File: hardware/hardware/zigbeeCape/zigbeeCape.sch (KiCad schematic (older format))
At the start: 46 parts

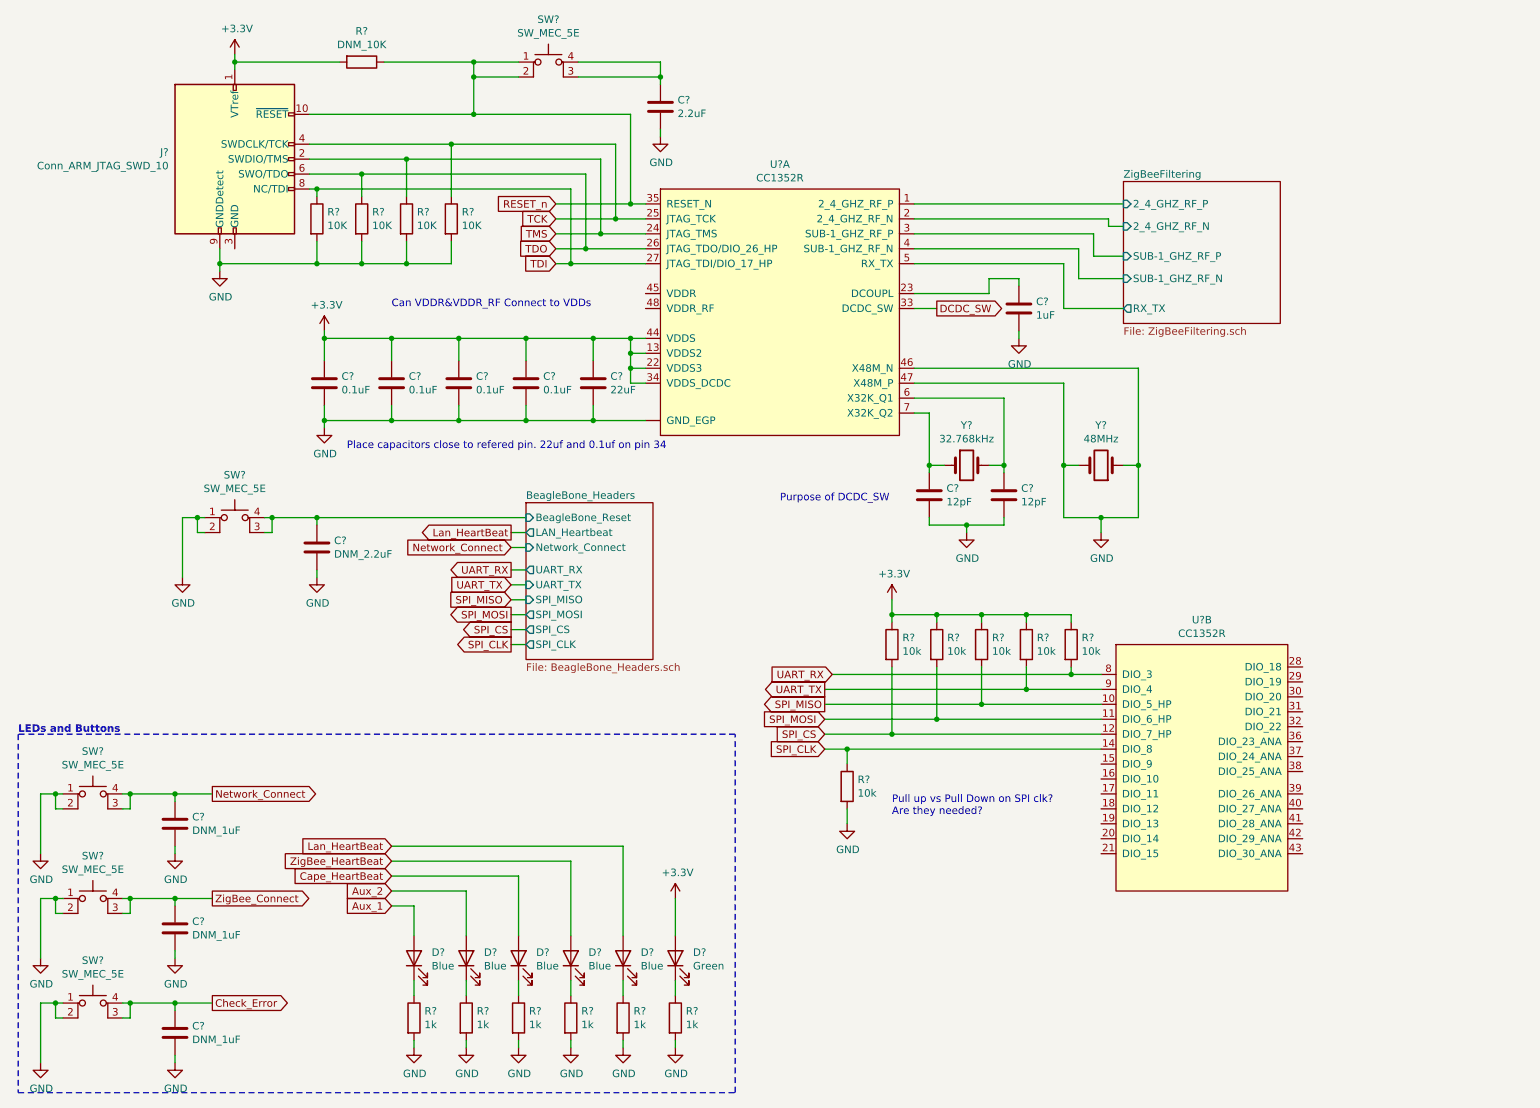
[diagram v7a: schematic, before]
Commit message: Added I2C pins, added signal wires to zigbee micro, fixed reset pin error
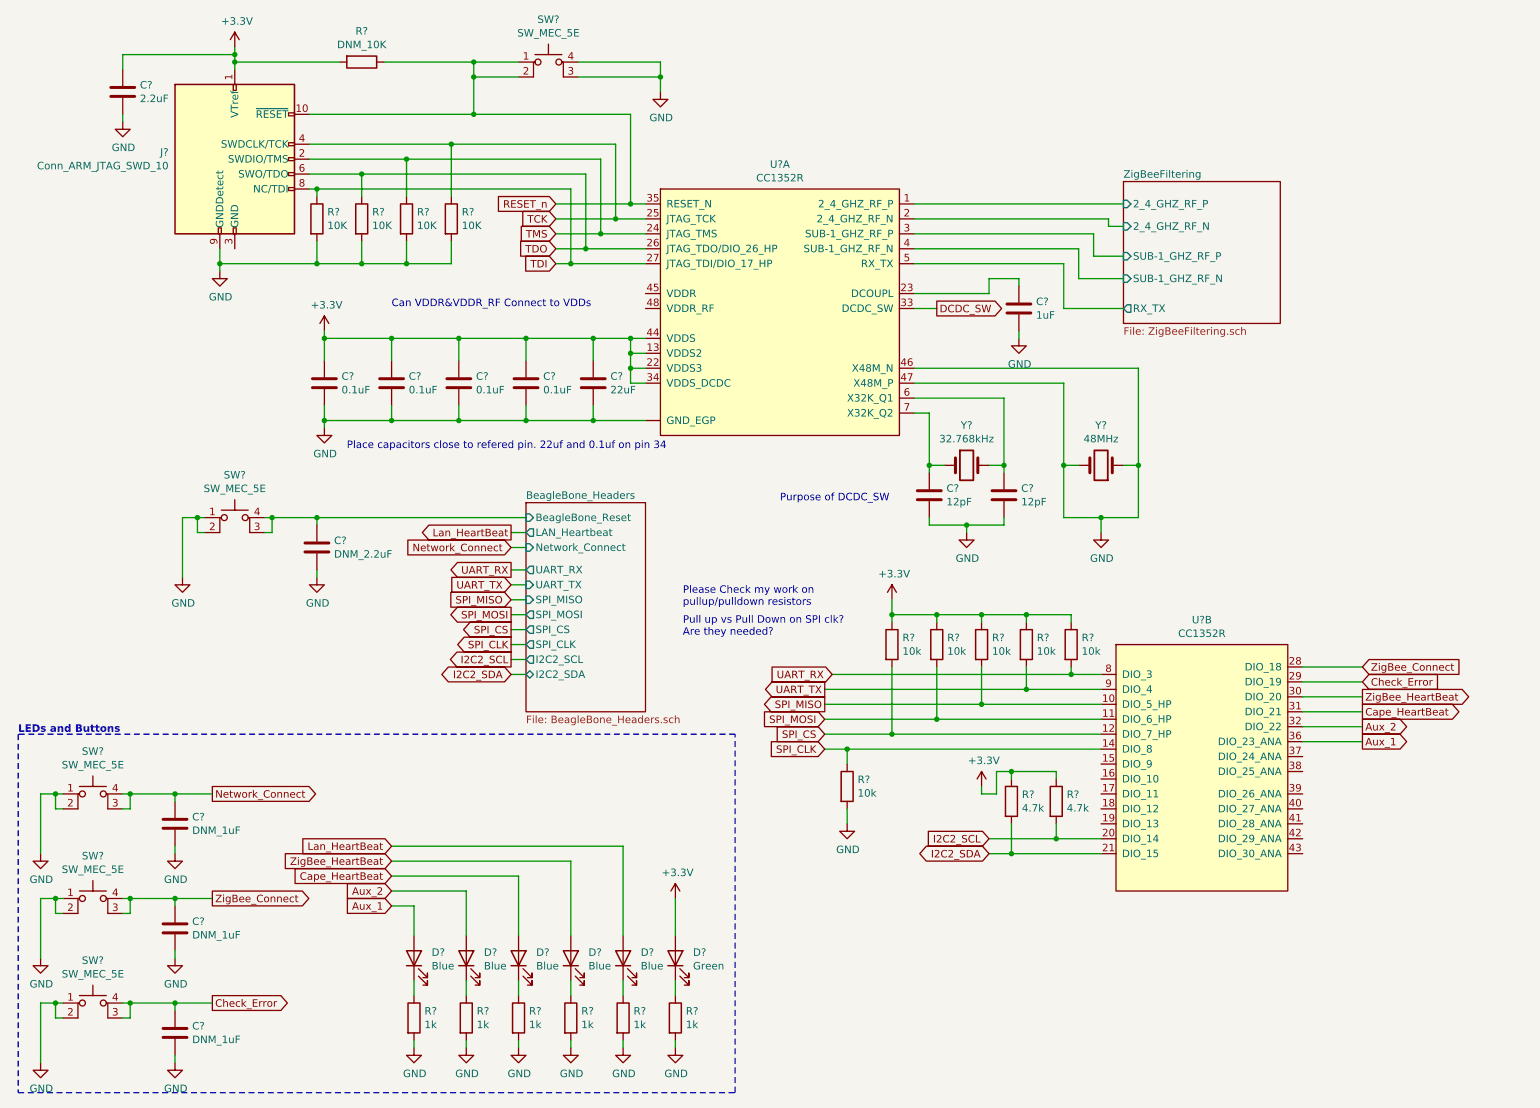
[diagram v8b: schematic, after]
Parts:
- added R? (x2): 4.7k, symbol Device:R
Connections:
- net +3V3: now also C?.1, R?.1, R?.1
- net Aux_1: now also U?.36 (DIO_23_ANA)
- net Aux_2: now also U?.32 (DIO_22)
- net Cape_HeartBeat: now also U?.31 (DIO_21)
- net Check_Error: now also U?.29 (DIO_19)
- net GND: now also SW?.3 (K), SW?.4 (A)
- net ZigBee_Connect: now also U?.28 (DIO_18)
- net ZigBee_HeartBeat: now also U?.30 (DIO_20)
- net I2C2_SCL: now reaches U?.20 (DIO_14)
- net I2C2_SCL: now also R?.2
- net I2C2_SDA: now reaches U?.21 (DIO_15)
- net I2C2_SDA: now also R?.2
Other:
- note added: "Please Check my work on \npullup/pulldown resistors"
- moved on the sheet: C?
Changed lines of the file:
@@
 Purpose of DCDC_SW
 $Sheet
-S 4000 3750 850  1050
+S 4000 3750 800  1400
 U 6087B849
 F0 "BeagleBone_Headers" 50
@@
 F9 "UART_TX" I L 4000 4300 50
 F10 "SPI_CLK" O L 4000 4700 50
+F11 "I2C2_SCL" O L 4000 4800 50
+F12 "I2C2_SDA" B L 4000 4900 50
 $EndSheet
 Wire Wire Line
@@
 	1    2900 800
 	0    1    1    0
-$EndComp
-$Comp
-L power:+3.3V #PWR?
-U 1 1 608A2617
-P 2050 750
-F 0 "#PWR?" H 2050 600 50  0001 C CNN
-F 1 "+3.3V" H 2065 923 50  0000 C CNN
-F 2 "" H 2050 750 50  0001 C CNN
-F 3 "" H 2050 750 50  0001 C CNN
-	1    2050 750
-	1    0    0    -1
 $EndComp
 $Comp
@@
 	4200 1850 4600 1850
 Connection ~ 4600 1850
-Wire Wire Line
-	2050 850  2050 800
 Connection ~ 3100 2650
 Connection ~ 3100 3200
@@
 Wire Wire Line
 	2550 1150 3650 1150
-Wire Wire Line
-	2050 800  2750 800
-Connection ~ 2050 800
-Wire Wire Line
-	2050 800  2050 750
 Wire Wire Line
 	3050 800  3650 800
@@
 L Device:C C?
 U 1 1 60A4B344
-P 4900 1100
-F 0 "C?" H 5015 1146 50  0000 L CNN
-F 1 "2.2uF" H 5015 1055 50  0000 L CNN
-F 2 "" H 4938 950 50  0001 C CNN
-F 3 "~" H 4900 1100 50  0001 C CNN
-	1    4900 1100
+P 1300 1000
+F 0 "C?" H 1415 1046 50  0000 L CNN
+F 1 "2.2uF" H 1415 955 50  0000 L CNN
+F 2 "" H 1338 850 50  0001 C CNN
+F 3 "~" H 1300 1000 50  0001 C CNN
+	1    1300 1000
 	1    0    0    -1
 $EndComp
 Wire Wire Line
 	4350 900  4900 900
-Wire Wire Line
-	4900 900  4900 950
 $Comp
 L power:GND #PWR?
 U 1 1 60A55AE5
-P 4900 1300
-F 0 "#PWR?" H 4900 1050 50  0001 C CNN
-F 1 "GND" H 4905 1127 50  0000 C CNN
-F 2 "" H 4900 1300 50  0001 C CNN
-F 3 "" H 4900 1300 50  0001 C CNN
-	1    4900 1300
-	1    0    0    -1
-$EndComp
-Wire Wire Line
-	4900 1300 4900 1250
+P 4900 1000
+F 0 "#PWR?" H 4900 750 50  0001 C CNN
+F 1 "GND" H 4905 827 50  0000 C CNN
+F 2 "" H 4900 1000 50  0001 C CNN
+F 3 "" H 4900 1000 50  0001 C CNN
+	1    4900 1000
+	1    0    0    -1
+$EndComp
 Wire Wire Line
 	4350 800  4900 800
 Wire Wire Line
 	4900 800  4900 900
-Connection ~ 4900 900
 $Comp
 L Switch:SW_MEC_5E SW?
@@
 Text GLabel 6000 5400 0    50   Input ~ 0
 SPI_CLK
-Text Notes 6450 5850 0    50   ~ 0
+Text Notes 5050 4650 0    50   ~ 0
 Pull up vs Pull Down on SPI clk?\nAre they needed?
-$Comp
-L Device:R R?
-U 1 1 60B56235
-P 7650 4700
-F 0 "R?" H 7720 4746 50  0000 L CNN
-F 1 "10k" H 7720 4655 50  0000 L CNN
-F 2 "" V 7580 4700 50  0001 C CNN
-F 3 "~" H 7650 4700 50  0001 C CNN
-	1    7650 4700
-	1    0    0    -1
-$EndComp
 $Comp
 L Device:R R?
@@
 Text Notes 2800 3400 0    50   ~ 0
 Place capacitors close to refered pin. 22uf and 0.1uf on pin 34
+Text GLabel 3900 4800 0    50   Output ~ 0
+I2C2_SCL
+Text GLabel 3900 4900 0    50   BiDi ~ 0
+I2C2_SDA
+Wire Wire Line
+	3900 4800 4000 4800
+Wire Wire Line
+	4000 4900 3900 4900
+$Comp
+L Device:R R?
+U 1 1 60B56235
+P 7650 4700
+F 0 "R?" H 7720 4746 50  0000 L CNN
+F 1 "10k" H 7720 4655 50  0000 L CNN
+F 2 "" V 7580 4700 50  0001 C CNN
+F 3 "~" H 7650 4700 50  0001 C CNN
+	1    7650 4700
+	1    0    0    -1
+$EndComp
+Text Notes 5050 4450 0    50   ~ 0
+Please Check my work on \npullup/pulldown resistors
+$Comp
+L Device:R R?
+U 1 1 608B8299
+P 7550 5750
+F 0 "R?" H 7620 5796 50  0000 L CNN
+F 1 "4.7k" H 7620 5705 50  0000 L CNN
+F 2 "" V 7480 5750 50  0001 C CNN
+F 3 "~" H 7550 5750 50  0001 C CNN
+	1    7550 5750
+	1    0    0    -1
+$EndComp
+$Comp
+L Device:R R?
+U 1 1 608B8AB3
+P 7250 5750
+F 0 "R?" H 7320 5796 50  0000 L CNN
+F 1 "4.7k" H 7320 5705 50  0000 L CNN
+F 2 "" V 7180 5750 50  0001 C CNN
+F 3 "~" H 7250 5750 50  0001 C CNN
+	1    7250 5750
+	1    0    0    -1
+$EndComp
+$Comp
+L power:+3.3V #PWR?
+U 1 1 608BA24C
+P 7050 5650
+F 0 "#PWR?" H 7050 5500 50  0001 C CNN
+F 1 "+3.3V" H 7065 5823 50  0000 C CNN
+F 2 "" H 7050 5650 50  0001 C CNN
+F 3 "" H 7050 5650 50  0001 C CNN
+	1    7050 5650
+	1    0    0    -1
+$EndComp
+Wire Wire Line
+	7550 5600 7550 5550
+Wire Wire Line
+	7550 5550 7250 5550
+Wire Wire Line
+	7250 5550 7250 5600
+Wire Wire Line
+	7250 5550 7150 5550
+Wire Wire Line
+	7150 5550 7150 5700
+Wire Wire Line
+	7150 5700 7050 5700
+Wire Wire Line
+	7050 5700 7050 5650
+Connection ~ 7250 5550
+Wire Wire Line
+	7850 6000 7550 6000
+Wire Wire Line
+	7550 6000 7550 5900
+Wire Wire Line
+	7850 6100 7250 6100
+Wire Wire Line
+	7250 6100 7250 5900
+Text GLabel 7100 6000 0    50   Input ~ 0
+I2C2_SCL
+Text GLabel 7100 6100 0    50   BiDi ~ 0
+I2C2_SDA
+Wire Wire Line
+	7550 6000 7100 6000
+Connection ~ 7550 6000
+Wire Wire Line
+	7250 6100 7100 6100
+Connection ~ 7250 6100
+$Comp
+L power:GND #PWR?
+U 1 1 609261BE
+P 1300 1200
+F 0 "#PWR?" H 1300 950 50  0001 C CNN
+F 1 "GND" H 1305 1027 50  0000 C CNN
+F 2 "" H 1300 1200 50  0001 C CNN
+F 3 "" H 1300 1200 50  0001 C CNN
+	1    1300 1200
+	1    0    0    -1
+$EndComp
+$Comp
+L power:+3.3V #PWR?
+U 1 1 608A2617
+P 2050 700
+F 0 "#PWR?" H 2050 550 50  0001 C CNN
+F 1 "+3.3V" H 2065 873 50  0000 C CNN
+F 2 "" H 2050 700 50  0001 C CNN
+F 3 "" H 2050 700 50  0001 C CNN
+	1    2050 700
+	1    0    0    -1
+$EndComp
+Wire Wire Line
+	2050 700  2050 750
+Wire Wire Line
+	2050 800  2750 800
+Wire Wire Line
+	2050 850  2050 800
+Connection ~ 2050 800
+Wire Wire Line
+	2050 750  1300 750
+Wire Wire Line
+	1300 750  1300 850
+Connection ~ 2050 750
+Wire Wire Line
+	2050 750  2050 800
+Wire Wire Line
+	1300 1200 1300 1150
+Wire Wire Line
+	4900 900  4900 1000
+Connection ~ 4900 900
+Text GLabel 9600 4850 2    50   Input ~ 0
+ZigBee_Connect
+Text GLabel 9600 4950 2    50   Input ~ 0
+Check_Error
+Text GLabel 9600 5050 2    50   Output ~ 0
+ZigBee_HeartBeat
+Text GLabel 9600 5150 2    50   Output ~ 0
+Cape_HeartBeat
+Text GLabel 9600 5250 2    50   Output ~ 0
+Aux_2
+Text GLabel 9600 5350 2    50   Output ~ 0
+Aux_1
+Wire Wire Line
+	9600 5350 9200 5350
+Wire Wire Line
+	9600 5250 9200 5250
+Wire Wire Line
+	9600 5150 9200 5150
+Wire Wire Line
+	9600 5050 9200 5050
+Wire Wire Line
+	9600 4950 9200 4950
+Wire Wire Line
+	9600 4850 9200 4850
 $EndSCHEMATC
